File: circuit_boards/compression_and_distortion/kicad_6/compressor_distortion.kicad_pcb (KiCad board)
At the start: 2 copper layers, 52.1 x 185.4 mm, 113 parts, among them J1 dry_in, J2 vcf_board_send_receive, J3 final_out, J4 power_entry, Q1 BS170, Q2 BF245A, Q3 BS170, Q4 BF245A, SW1 bypass_switch_A, SW2 bypass_switch_B, U1 TL072, U2 NE570, U3 TL072, U4 TL072, U5 TL072, U6 TL072

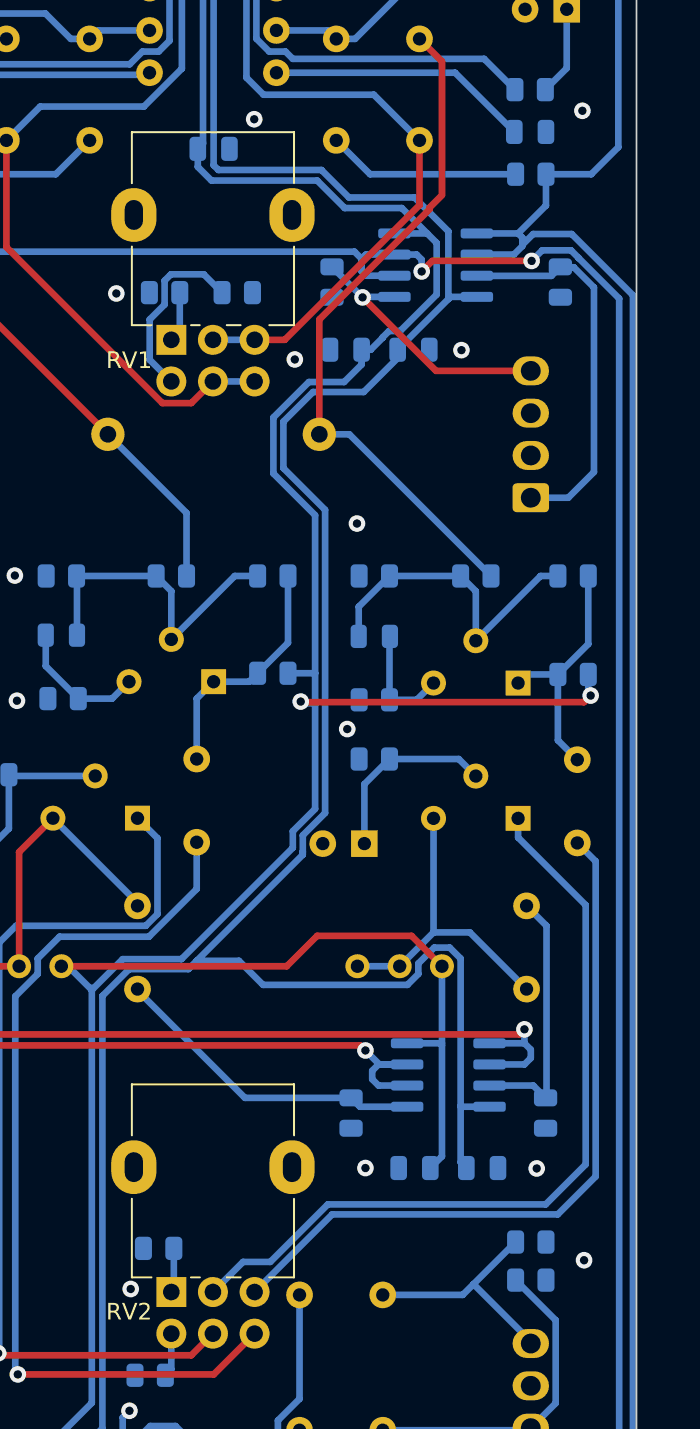
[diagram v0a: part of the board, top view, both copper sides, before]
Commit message: Fix a/b swap error and dim LED error
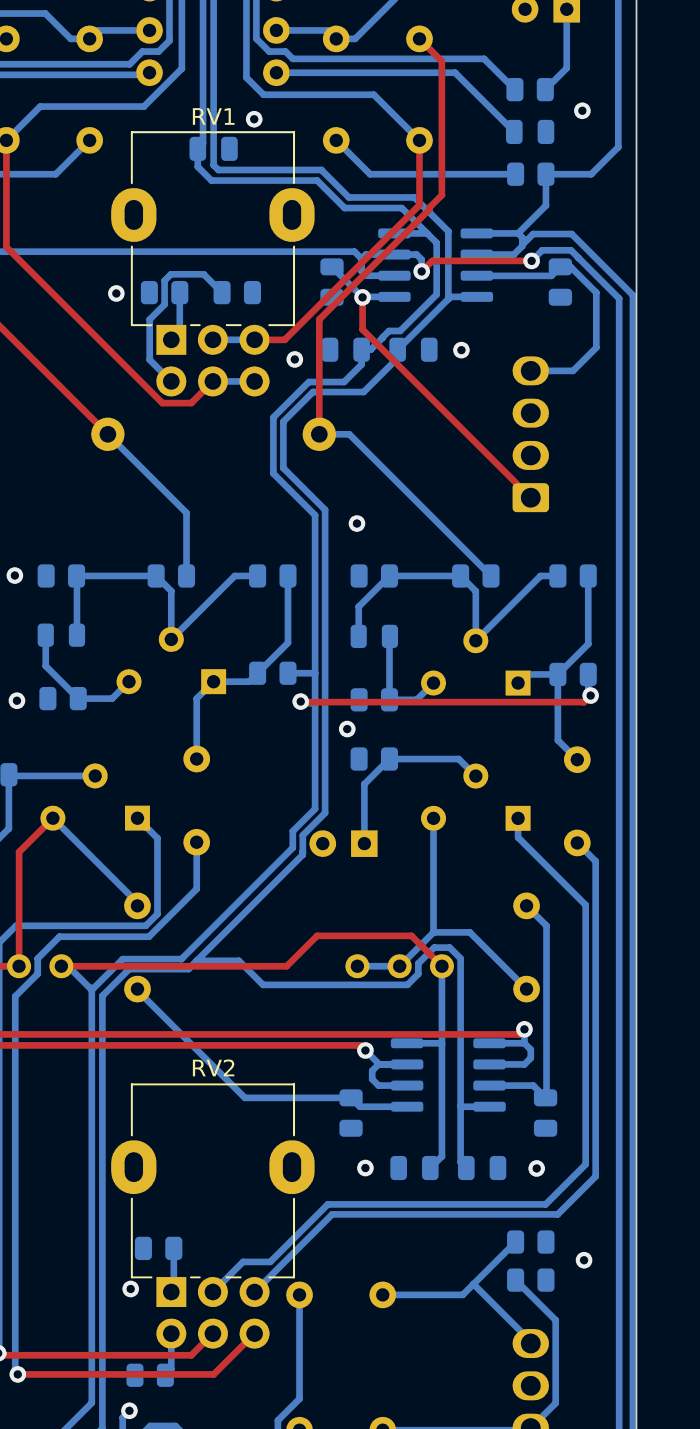
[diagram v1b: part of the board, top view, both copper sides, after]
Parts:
- R44, R45: value 3k3 -> 100
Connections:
- J1 pad 1: /input_buffer_A/SIGNAL_IN -> /input_buffer_B/SIGNAL_IN
- J1 pad 4: /input_buffer_B/SIGNAL_IN -> /input_buffer_A/SIGNAL_IN
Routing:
- net /input_buffer_A/SIGNAL_IN: track 23.3 -> 15.9 mm
- net /input_buffer_B/SIGNAL_IN: track 16.5 -> 20.7 mm

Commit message: Update silkscreen to match rev and date
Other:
- board text added: "Compressor and Distortion board rev 0.1 2023-04-15"
- board text removed: "Compressor and Distortion board rev 0 2022-05-22"
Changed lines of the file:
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@@
     (effects (font (size 1 1) (thickness 0.15)) (justify left mirror))
   )
-  (gr_text "Compressor and\nDistortion board\nrev 0\n2022-05-22" (at 132.715 52.705) (layer "B.SilkS")
+  (gr_text "Compressor and\nDistortion board\nrev 0.1\n2023-04-15" (at 132.715 52.705) (layer "B.SilkS")
     (effects (font (size 1 1) (thickness 0.15)) (justify left mirror))
   )
